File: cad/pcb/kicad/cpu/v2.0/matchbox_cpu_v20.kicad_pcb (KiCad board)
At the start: 6 copper layers, 40 x 66 mm, 83 parts, among them P1 DF12-32-DP, P2 DF12-32-DP, P3 DF12-32-DP, P4 DF12-32-DP, Q1 FDN360P, Q2 FDN360P, SW0 BOOT0, SW1 B3U-3100PM-B, SW2 B3U-3100PM-B, SW3 RESET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

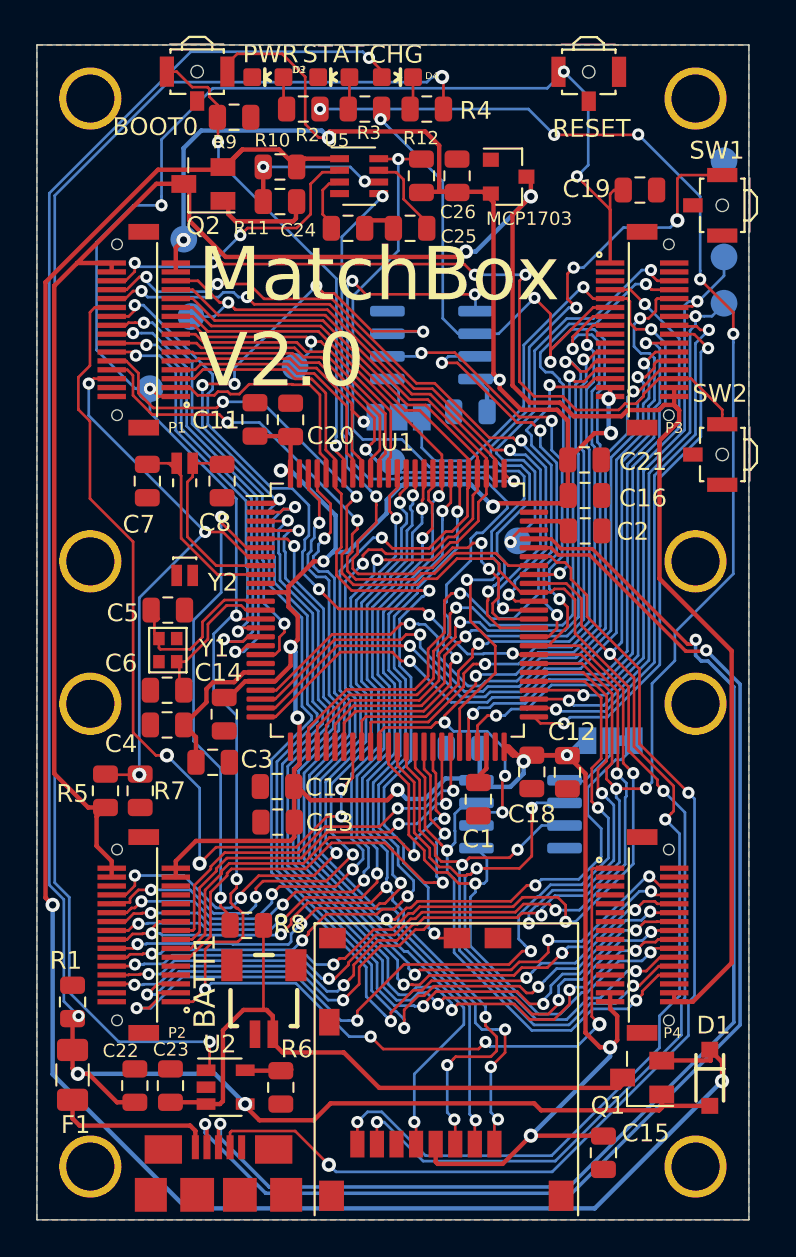
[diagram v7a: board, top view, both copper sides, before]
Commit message: Looks like P2 & P3 got swapped again. Flip them back.
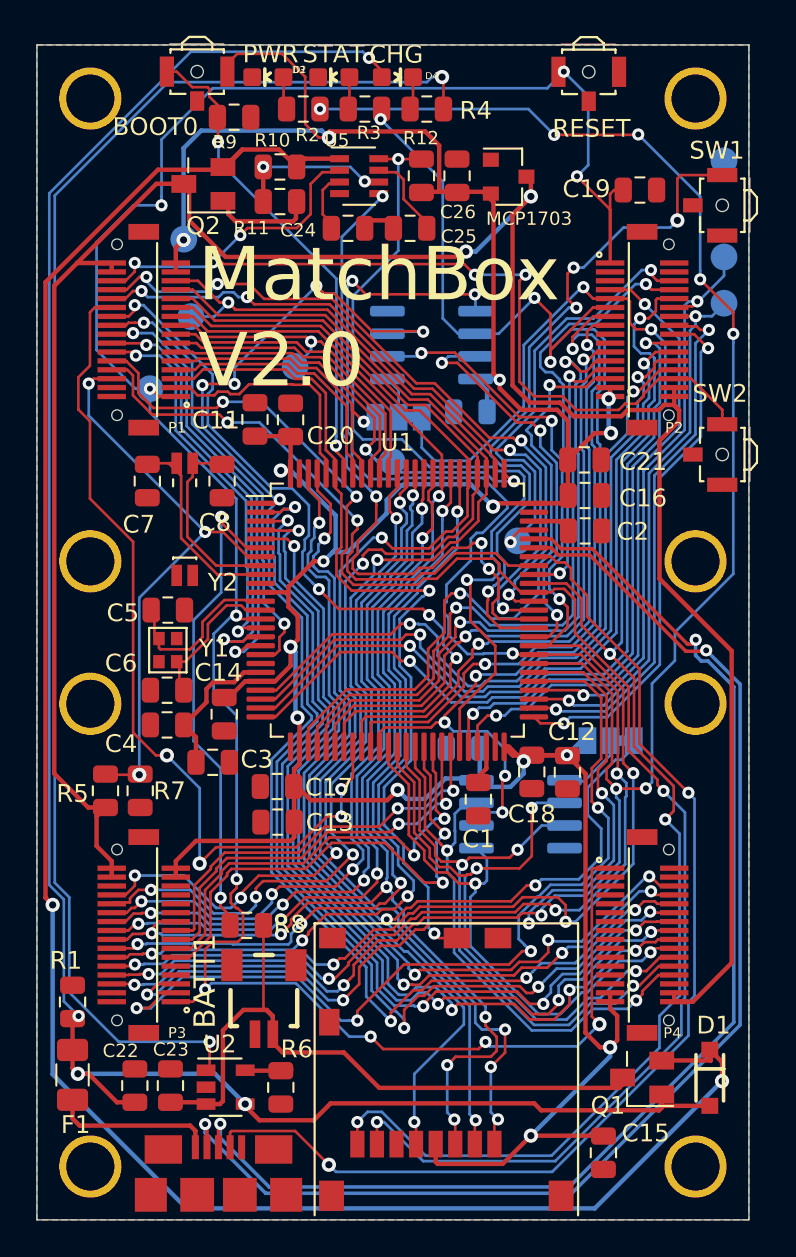
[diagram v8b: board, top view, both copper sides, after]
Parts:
- renumbered P3 to P2, P2 to P3
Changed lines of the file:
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@@
     (4 Route15 signal)
     (31 Bottom signal)
-    (32 B.Adhes user hide)
-    (33 F.Adhes user hide)
-    (34 B.Paste user hide)
-    (35 F.Paste user hide)
-    (36 B.SilkS user hide)
-    (37 F.SilkS user hide)
-    (38 B.Mask user hide)
-    (39 F.Mask user hide)
-    (40 Dwgs.User user hide)
-    (41 Cmts.User user hide)
-    (42 Eco1.User user hide)
-    (43 Eco2.User user hide)
-    (44 Edge.Cuts user hide)
-    (45 Margin user hide)
-    (46 B.CrtYd user hide)
-    (47 F.CrtYd user hide)
-    (48 B.Fab user hide)
-    (49 F.Fab user hide)
+    (32 B.Adhes user)
+    (33 F.Adhes user)
+    (34 B.Paste user)
+    (35 F.Paste user)
+    (36 B.SilkS user)
+    (37 F.SilkS user)
+    (38 B.Mask user)
+    (39 F.Mask user)
+    (40 Dwgs.User user)
+    (41 Cmts.User user)
+    (42 Eco1.User user)
+    (43 Eco2.User user)
+    (44 Edge.Cuts user)
+    (45 Margin user)
+    (46 B.CrtYd user)
+    (47 F.CrtYd user)
+    (48 B.Fab user)
+    (49 F.Fab user)
   )
   (setup
-    (last_trace_width 0.1524)
+    (last_trace_width 0.25)
     (user_trace_width 0.1524)
     (user_trace_width 0.254)
@@
   (net 120 "Net-(C24-Pad1)")
   (net 121 "Net-(C25-Pad1)")
-  (net 122 "Net-(P2-Pad28)")
-  (net 123 "Net-(P2-Pad27)")
-  (net 124 "Net-(P2-Pad25)")
-  (net 125 "Net-(P2-Pad23)")
-  (net 126 "Net-(P2-Pad21)")
-  (net 127 "Net-(P2-Pad9)")
-  (net 128 "Net-(P2-Pad7)")
-  (net 129 "Net-(P3-Pad19)")
-  (net 130 "Net-(P3-Pad17)")
-  (net 131 "Net-(P3-Pad5)")
-  (net 132 "Net-(P3-Pad3)")
-  (net 133 "Net-(SW3-PadGND)")
+  (net 122 "Net-(SW3-PadGND)")
+  (net 123 "Net-(P2-Pad19)")
+  (net 124 "Net-(P2-Pad17)")
+  (net 125 "Net-(P2-Pad5)")
+  (net 126 "Net-(P2-Pad3)")
+  (net 127 "Net-(P3-Pad28)")
+  (net 128 "Net-(P3-Pad27)")
+  (net 129 "Net-(P3-Pad25)")
+  (net 130 "Net-(P3-Pad23)")
+  (net 131 "Net-(P3-Pad21)")
+  (net 132 "Net-(P3-Pad9)")
+  (net 133 "Net-(P3-Pad7)")
   (net_class Default "This is the default net class."
     (clearance 0.1524)
@@
     (add_net "Net-(D3-PadA)")
     (add_net "Net-(D4-PadC)")
-    (add_net "Net-(P2-Pad21)")
-    (add_net "Net-(P2-Pad23)")
-    (add_net "Net-(P2-Pad25)")
-    (add_net "Net-(P2-Pad27)")
-    (add_net "Net-(P2-Pad28)")
-    (add_net "Net-(P2-Pad7)")
-    (add_net "Net-(P2-Pad9)")
-    (add_net "Net-(P3-Pad17)")
-    (add_net "Net-(P3-Pad19)")
-    (add_net "Net-(P3-Pad3)")
-    (add_net "Net-(P3-Pad5)")
+    (add_net "Net-(P2-Pad17)")
+    (add_net "Net-(P2-Pad19)")
+    (add_net "Net-(P2-Pad3)")
+    (add_net "Net-(P2-Pad5)")
+    (add_net "Net-(P3-Pad21)")
+    (add_net "Net-(P3-Pad23)")
+    (add_net "Net-(P3-Pad25)")
+    (add_net "Net-(P3-Pad27)")
+    (add_net "Net-(P3-Pad28)")
+    (add_net "Net-(P3-Pad7)")
+    (add_net "Net-(P3-Pad9)")
     (add_net "Net-(P4-Pad11)")
     (add_net "Net-(P4-Pad13)")
@@
     (at 34 -50.01 270)
     (descr "Hirose DF12 Pattern with metal fitting, 32 positions")
-    (fp_text reference P3 (at 5.51 -1.8) (layer F.SilkS)
+    (fp_text reference P2 (at 5.51 -1.8) (layer F.SilkS)
       (effects (font (size 0.60325 0.60325) (thickness 0.04826)))
     )
@@
       (net 39 /PA3) (solder_mask_margin 0.0762))
     (pad 19 smd rect (at 0.75 1.8001 270) (size 0.3 1.6) (layers Top F.Mask)
-      (net 129 "Net-(P3-Pad19)") (solder_mask_margin 0.0762))
+      (net 123 "Net-(P2-Pad19)") (solder_mask_margin 0.0762))
     (pad 18 smd rect (at 0.25 -1.8001 270) (size 0.3 1.6) (layers Top F.Mask)
       (net 27 /PB12) (solder_mask_margin 0.0762))
     (pad 17 smd rect (at 0.25 1.8001 270) (size 0.3 1.6) (layers Top F.Mask)
-      (net 130 "Net-(P3-Pad17)") (solder_mask_margin 0.0762))
+      (net 124 "Net-(P2-Pad17)") (solder_mask_margin 0.0762))
     (pad 16 smd rect (at -0.25 -1.8001 270) (size 0.3 1.6) (layers Top F.Mask)
       (net 26 /PB13) (solder_mask_margin 0.0762))
@@
       (net 17 /PA13) (solder_mask_margin 0.0762))
     (pad 5 smd rect (at -2.75 1.8001 270) (size 0.3 1.6) (layers Top F.Mask)
-      (net 131 "Net-(P3-Pad5)") (solder_mask_margin 0.0762))
+      (net 125 "Net-(P2-Pad5)") (solder_mask_margin 0.0762))
     (pad 4 smd rect (at -3.25 -1.8001 270) (size 0.3 1.6) (layers Top F.Mask)
       (net 1 GND) (solder_mask_margin 0.0762))
     (pad 3 smd rect (at -3.25 1.8001 270) (size 0.3 1.6) (layers Top F.Mask)
-      (net 132 "Net-(P3-Pad3)") (solder_mask_margin 0.0762))
+      (net 126 "Net-(P2-Pad3)") (solder_mask_margin 0.0762))
     (pad 2 smd rect (at -3.75 -1.8001 270) (size 0.3 1.6) (layers Top F.Mask)
       (net 1 GND) (solder_mask_margin 0.0762))
@@
     (fp_line (start -1.5 -1.25) (end -1.5 -1.05) (layer F.SilkS) (width 0.127))
     (pad GND smd rect (at 0 1.65) (size 0.8 1.1) (layers Top F.Paste F.Mask)
-      (net 133 "Net-(SW3-PadGND)") (solder_mask_margin 0.0762))
+      (net 122 "Net-(SW3-PadGND)") (solder_mask_margin 0.0762))
     (pad "" np_thru_hole circle (at 0 0) (size 0.7 0.7) (drill 0.7) (layers *.Cu *.Mask))
     (pad 2 smd rect (at 1.7 0) (size 0.8 1.7) (layers Top F.Paste F.Mask)
@@
     (at 6 -16.01 90)
     (descr "Hirose DF12 Pattern with metal fitting, 32 positions")
-    (fp_text reference P2 (at -5.5 1.875 180) (layer F.SilkS)
+    (fp_text reference P3 (at -5.5 1.875 180) (layer F.SilkS)
       (effects (font (size 0.60325 0.60325) (thickness 0.04826)))
     )
@@
       (net 2 /VCC_3V3) (solder_mask_margin 0.0762))
     (pad 28 smd rect (at 2.75 -1.8001 90) (size 0.3 1.6) (layers Top F.Mask)
-      (net 122 "Net-(P2-Pad28)") (solder_mask_margin 0.0762))
+      (net 127 "Net-(P3-Pad28)") (solder_mask_margin 0.0762))
     (pad 27 smd rect (at 2.75 1.8001 90) (size 0.3 1.6) (layers Top F.Mask)
-      (net 123 "Net-(P2-Pad27)") (solder_mask_margin 0.0762))
+      (net 128 "Net-(P3-Pad27)") (solder_mask_margin 0.0762))
     (pad 26 smd rect (at 2.25 -1.8001 90) (size 0.3 1.6) (layers Top F.Mask)
       (net 65 /PD7) (solder_mask_margin 0.0762))
     (pad 25 smd rect (at 2.25 1.8001 90) (size 0.3 1.6) (layers Top F.Mask)
-      (net 124 "Net-(P2-Pad25)") (solder_mask_margin 0.0762))
+      (net 129 "Net-(P3-Pad25)") (solder_mask_margin 0.0762))
     (pad 24 smd rect (at 1.75 -1.8001 90) (size 0.3 1.6) (layers Top F.Mask)
       (net 66 /PD6) (solder_mask_margin 0.0762))
     (pad 23 smd rect (at 1.75 1.8001 90) (size 0.3 1.6) (layers Top F.Mask)
-      (net 125 "Net-(P2-Pad23)") (solder_mask_margin 0.0762))
+      (net 130 "Net-(P3-Pad23)") (solder_mask_margin 0.0762))
     (pad 22 smd rect (at 1.25 -1.8001 90) (size 0.3 1.6) (layers Top F.Mask)
       (net 67 /PD5) (solder_mask_margin 0.0762))
     (pad 21 smd rect (at 1.25 1.8001 90) (size 0.3 1.6) (layers Top F.Mask)
-      (net 126 "Net-(P2-Pad21)") (solder_mask_margin 0.0762))
+      (net 131 "Net-(P3-Pad21)") (solder_mask_margin 0.0762))
     (pad 20 smd rect (at 0.75 -1.8001 90) (size 0.3 1.6) (layers Top F.Mask)
       (net 68 /PD4) (solder_mask_margin 0.0762))
@@
       (net 75 /PD12) (solder_mask_margin 0.0762))
     (pad 9 smd rect (at -1.75 1.8001 90) (size 0.3 1.6) (layers Top F.Mask)
-      (net 127 "Net-(P2-Pad9)") (solder_mask_margin 0.0762))
+      (net 132 "Net-(P3-Pad9)") (solder_mask_margin 0.0762))
     (pad 8 smd rect (at -2.25 -1.8001 90) (size 0.3 1.6) (layers Top F.Mask)
       (net 76 /PD11) (solder_mask_margin 0.0762))
     (pad 7 smd rect (at -2.25 1.8001 90) (size 0.3 1.6) (layers Top F.Mask)
-      (net 128 "Net-(P2-Pad7)") (solder_mask_margin 0.0762))
+      (net 133 "Net-(P3-Pad7)") (solder_mask_margin 0.0762))
     (pad 6 smd rect (at -2.75 -1.8001 90) (size 0.3 1.6) (layers Top F.Mask)
       (net 77 /PD10) (solder_mask_margin 0.0762))
